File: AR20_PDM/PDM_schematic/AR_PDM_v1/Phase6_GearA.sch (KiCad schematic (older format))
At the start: 12 parts, among them Q5 BTS50025-1TAD, U10 N-MOS, U5 INA233

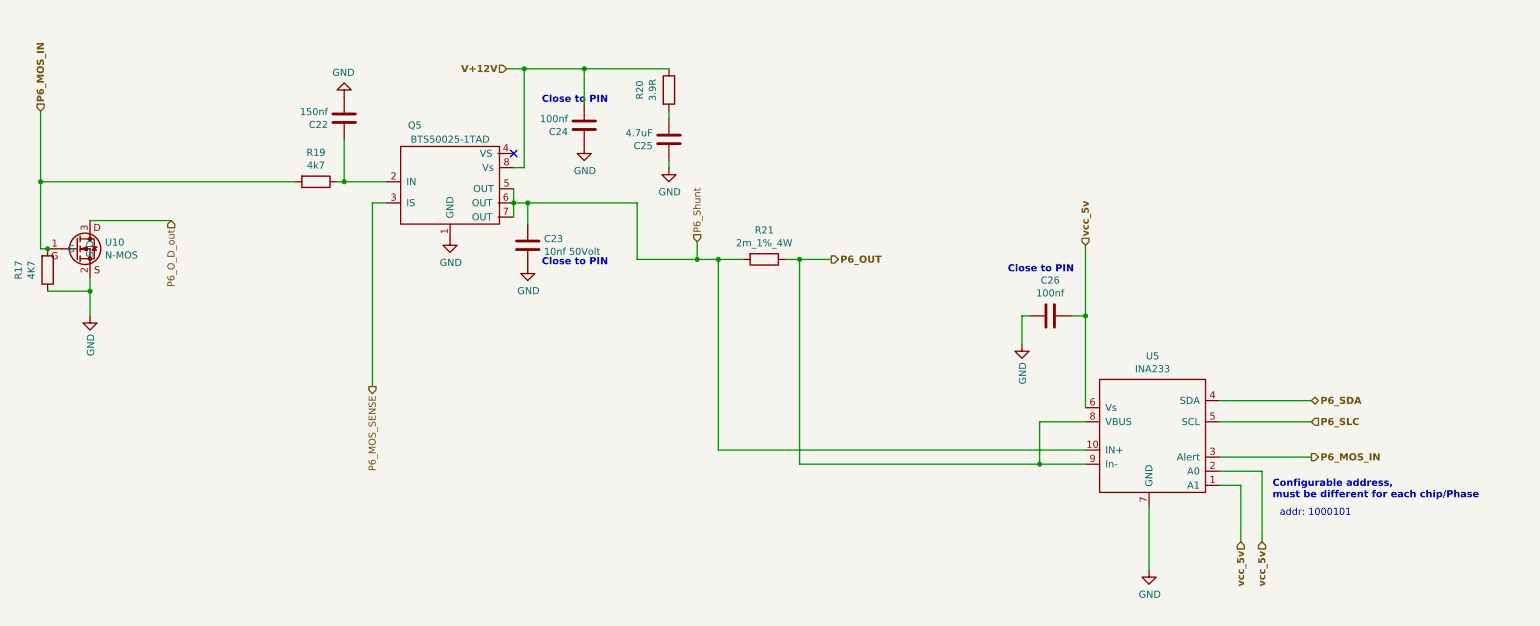
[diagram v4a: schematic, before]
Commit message: schematics rework
Fixed INA233 frying due to inductive flyback:
- Paced ina233 high side of the mosftets
- New input protection reseistors, and zener diodes, on each ina233.
Simplified:
- Removed the MUX and mos sense lines, as i realize that most of this functionality can be obtained trough INA233.
- Removed some of the cappacitors , besides the most needed ones.
- removed  back to back zener diode configuration, now a single diode insted.
 to reduce negative voltage in case of loss of VS, to be easy on the INA233 filters.
new stuff:
- Another temp sensor.
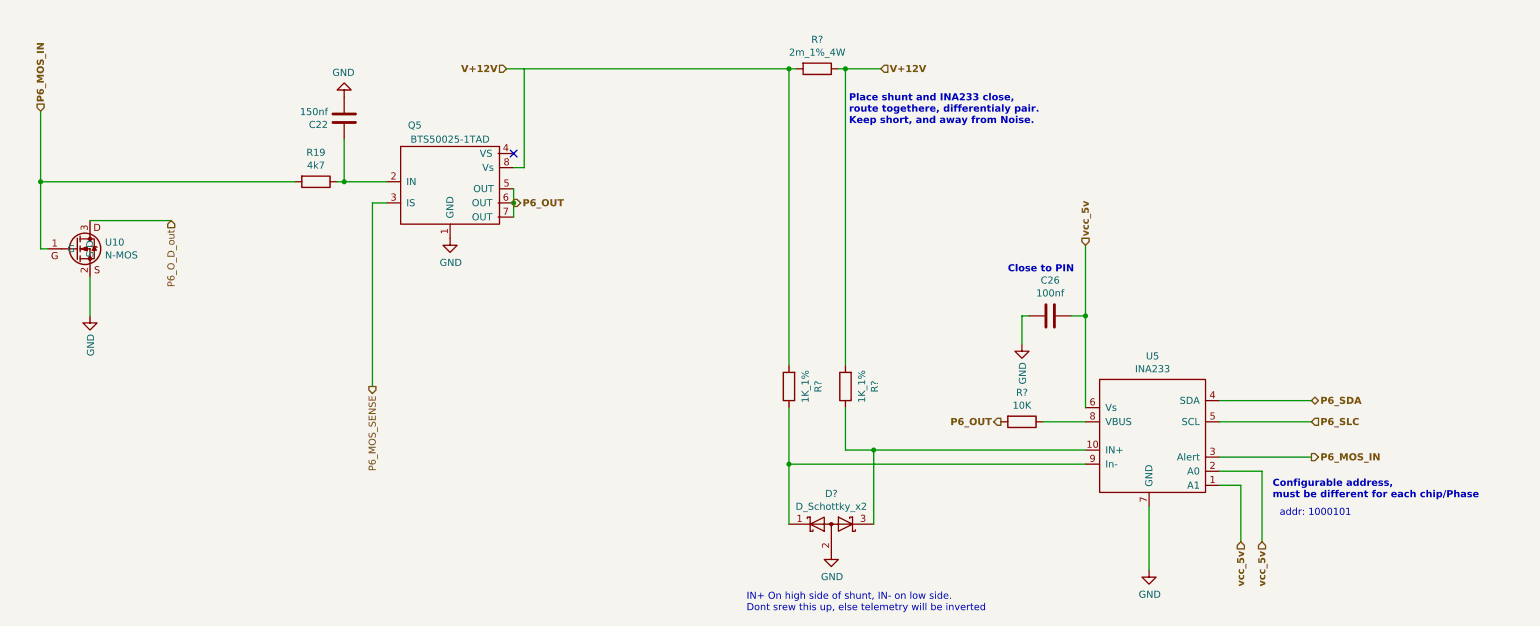
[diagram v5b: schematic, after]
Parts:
- removed C23: 10nf 50Volt, Capacitor_SMD:C_0603_1608Metric, symbol AR20_PDM_v1-rescue:C-Device
- removed C24: 100nf, Capacitor_SMD:C_0603_1608Metric, symbol AR20_PDM_v1-rescue:C-Device
- removed C25: 4.7uF, Capacitor_SMD:C_1206_3216Metric, symbol AR20_PDM_v1-rescue:C-Device
- removed R17: 4K7, Resistor_SMD:R_0603_1608Metric, symbol AR20_PDM_v1-rescue:R-Device
- removed R20: 3.9R, Resistor_SMD:R_2512_6332Metric, symbol AR20_PDM_v1-rescue:R-Device
- removed R21: 2m_1%_4W, Resistor_SMD:R_2512_6332Metric, symbol AR20_PDM_v1-rescue:R-Device
- added D?: D_Schottky_x2, symbol AR20_PDM_v1-rescue:D_Schottky_x2
- added R?: 2m_1%_4W, Resistor_SMD:R_2512_6332Metric, symbol AR20_PDM_v1-rescue:R-Device
- added R? (x2): 1K_1%, Resistor_SMD:R_0603_1608Metric, symbol AR20_PDM_v1-rescue:R-Device
- added R?: 10K, Resistor_SMD:R_0603_1608Metric, symbol AR20_PDM_v1-rescue:R-Device
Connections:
- net GND: now also D?.2 (A)
- net P6_OUT: now also Q5.5 (OUT), Q5.6 (OUT), Q5.7 (OUT), R?.2; no longer U5.8 (VBUS), U5.9 (In-)
- net V+12V: now also R?.1, R?.2, R?.2, R?.2
- removed net P6_Shunt: Q5.5 (OUT), Q5.6 (OUT), Q5.7 (OUT), U5.10 (IN+)
- new net: D?.3 (K), R?.1, U5.10 (IN+)
- new net: R?.1, U5.8 (VBUS)
- new net: D?.1 (K), R?.1, U5.9 (In-)
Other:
- note added: "IN+ On high side of shunt, IN- on low side.\nDont srew this up, else telemetry will be inverted"
- note added: "Place shunt and INA233 close, \nroute togethere, differentialy pair. \nKeep short, and away from Noise."

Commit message: Working on pcb layout
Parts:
- removed D?: D_Schottky_x2, symbol AR20_PDM_v1-rescue:D_Schottky_x2
- added D47, D49: D_Schottky_BAT60A, AR_PDM_v1:D_Shotky_BAT60_HandSoldering, symbol AR20_PDM_v1-rescue:D_Schottky_BAT60A
- gave numbers to parts that had none: 4
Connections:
- net GND: now also D47.2 (A), D49.2 (A)
- net V+12V: no longer Q5.8 (Vs), R32.2, R33.2
- net at R109.1, U5.10 (IN+): now also D49.1 (K)
- net at R32.1, U5.9 (In-): now also D47.1 (K)
- new net: Q5.8 (Vs), R32.2, R33.2
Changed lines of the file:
@@
 Connection ~ 1350 2400
-Wire Wire Line
-	4650 1600 4775 1600
 Wire Wire Line
 	4775 2300 4700 2300
@@
 Wire Wire Line
 	1700 3075 1700 3350
-Text HLabel 4650 1600 0    50   Input ~ 10
-V+12V
 Text HLabel 4700 2550 2    50   Output ~ 10
 P6_OUT
@@
 AR Path="/5E0FC3A2/5EEB3767" Ref="R?"  Part="1"
 AR Path="/5E0FCFDC/5EEB3767" Ref="R?"  Part="1"
-AR Path="/5E0FDCCC/5EEB3767" Ref="R?"  Part="1"
+AR Path="/5E0FDCCC/5EEB3767" Ref="R33"  Part="1"
 AR Path="/5E10174B/5EEB3767" Ref="R?"  Part="1"
-F 0 "R?" V 6643 1600 50  0000 C CNN
+F 0 "R33" V 6643 1600 50  0000 C CNN
 F 1 "2m_1%_4W" V 6734 1600 50  0000 C CNN
 F 2 "Resistor_SMD:R_2512_6332Metric" V 6780 1600 50  0001 C CNN
@@
 Text HLabel 7300 1600 2    50   Input ~ 10
 V+12V
-$Comp
-L AR20_PDM_v1-rescue:D_Schottky_x2 D?
-U 1 1 5EEB376E
-P 6950 4825
-AR Path="/5DA89415/5EEB376E" Ref="D?"  Part="1"
-AR Path="/5E0FDCCC/5EEB376E" Ref="D?"  Part="1"
-F 0 "D?" H 6950 5041 50  0000 C CNN
-F 1 "D_Schottky_x2" H 6950 4950 50  0000 C CNN
-F 2 "" H 6950 4825 50  0001 C CNN
-F 3 "~" H 6950 4825 50  0001 C CNN
-	1    6950 4825
-	1    0    0    -1
-$EndComp
 $Comp
 L AR20_PDM_v1-rescue:R-Device R?
@@
 AR Path="/5E0FC3A2/5EEB3774" Ref="R?"  Part="1"
 AR Path="/5E0FCFDC/5EEB3774" Ref="R?"  Part="1"
-AR Path="/5E0FDCCC/5EEB3774" Ref="R?"  Part="1"
+AR Path="/5E0FDCCC/5EEB3774" Ref="R32"  Part="1"
 AR Path="/5E10174B/5EEB3774" Ref="R?"  Part="1"
-F 0 "R?" V 6443 3850 50  0000 C CNN
+F 0 "R32" V 6443 3850 50  0000 C CNN
 F 1 "1K_1%" V 6534 3850 50  0000 C CNN
 F 2 "Resistor_SMD:R_0603_1608Metric" V 6580 3850 50  0001 C CNN
@@
 AR Path="/5E0FC3A2/5EEB377A" Ref="R?"  Part="1"
 AR Path="/5E0FCFDC/5EEB377A" Ref="R?"  Part="1"
-AR Path="/5E0FDCCC/5EEB377A" Ref="R?"  Part="1"
+AR Path="/5E0FDCCC/5EEB377A" Ref="R109"  Part="1"
 AR Path="/5E10174B/5EEB377A" Ref="R?"  Part="1"
-F 0 "R?" V 6843 3850 50  0000 C CNN
+F 0 "R109" V 6843 3850 50  0000 C CNN
 F 1 "1K_1%" V 6934 3850 50  0000 C CNN
 F 2 "Resistor_SMD:R_0603_1608Metric" V 6980 3850 50  0001 C CNN
@@
 Text Notes 7075 2000 0    50   ~ 10
 Place shunt and INA233 close, \nroute togethere, differentialy pair. \nKeep short, and away from Noise.
-$Comp
-L AR20_PDM_v1-rescue:GND-power #PWR?
-U 1 1 5EEB3788
-P 6950 5025
-AR Path="/5DA89415/5EEB3788" Ref="#PWR?"  Part="1"
-AR Path="/5DEB10A1/5EEB3788" Ref="#PWR?"  Part="1"
-AR Path="/5DEB20EA/5EEB3788" Ref="#PWR?"  Part="1"
-AR Path="/5E0E4725/5EEB3788" Ref="#PWR?"  Part="1"
-AR Path="/5E0E4A93/5EEB3788" Ref="#PWR?"  Part="1"
-AR Path="/5E0E4EB5/5EEB3788" Ref="#PWR?"  Part="1"
-AR Path="/5E0E5304/5EEB3788" Ref="#PWR?"  Part="1"
-AR Path="/5E0E594B/5EEB3788" Ref="#PWR?"  Part="1"
-AR Path="/5E0E607C/5EEB3788" Ref="#PWR?"  Part="1"
-AR Path="/5E0FB5C8/5EEB3788" Ref="#PWR?"  Part="1"
-AR Path="/5E0FBBBD/5EEB3788" Ref="#PWR?"  Part="1"
-AR Path="/5E0FC3A2/5EEB3788" Ref="#PWR?"  Part="1"
-AR Path="/5E0FCFDC/5EEB3788" Ref="#PWR?"  Part="1"
-AR Path="/5E0FDCCC/5EEB3788" Ref="#PWR?"  Part="1"
-AR Path="/5E10174B/5EEB3788" Ref="#PWR?"  Part="1"
-F 0 "#PWR?" H 6950 4775 50  0001 C CNN
-F 1 "GND" H 6955 4852 50  0000 C CNN
-F 2 "" H 6950 5025 50  0001 C CNN
-F 3 "" H 6950 5025 50  0001 C CNN
-	1    6950 5025
-	1    0    0    -1
-$EndComp
 Wire Wire Line
 	4775 1600 6650 1600
@@
 Wire Wire Line
 	6650 4400 8750 4400
-Connection ~ 6650 4400
-Wire Wire Line
-	6650 4400 6650 4825
-Wire Wire Line
-	8750 4300 7250 4300
-Wire Wire Line
-	7250 4825 7250 4300
-Connection ~ 7250 4300
-Wire Wire Line
-	7250 4300 7050 4300
 $Comp
 L AR20_PDM_v1-rescue:R-Device R?
@@
 AR Path="/5E0FC3A2/5EEC7147" Ref="R?"  Part="1"
 AR Path="/5E0FCFDC/5EEC7147" Ref="R?"  Part="1"
-AR Path="/5E0FDCCC/5EEC7147" Ref="R?"  Part="1"
+AR Path="/5E0FDCCC/5EEC7147" Ref="R110"  Part="1"
 AR Path="/5E10174B/5EEC7147" Ref="R?"  Part="1"
-F 0 "R?" V 8093 4100 50  0000 C CNN
+F 0 "R110" V 8093 4100 50  0000 C CNN
 F 1 "10K" V 8184 4100 50  0000 C CNN
 F 2 "Resistor_SMD:R_0603_1608Metric" V 8230 4100 50  0001 C CNN
@@
 Text HLabel 8150 4100 0    50   Output ~ 10
 P6_OUT
+Wire Wire Line
+	7050 4300 7100 4300
+$Comp
+L AR20_PDM_v1-rescue:D_Schottky_BAT60A D?
+U 1 1 5EFB12F9
+P 6700 4775
+AR Path="/5DA89415/5EFB12F9" Ref="D?"  Part="1"
+AR Path="/5E0FDCCC/5EFB12F9" Ref="D47"  Part="1"
+F 0 "D47" V 6530 4885 50  0000 L CNN
+F 1 "D_Schottky_BAT60A" V 6621 4885 50  0000 L CNN
+F 2 "AR_PDM_v1:D_Shotky_BAT60_HandSoldering" H 6800 4725 50  0001 C CNN
+F 3 "~" H 6800 4725 50  0001 C CNN
+	1    6700 4775
+	0    1    1    0
+$EndComp
+$Comp
+L AR20_PDM_v1-rescue:GND-power #PWR?
+U 1 1 5EFB12FF
+P 6875 4950
+AR Path="/5DA89415/5EFB12FF" Ref="#PWR?"  Part="1"
+AR Path="/5DEB10A1/5EFB12FF" Ref="#PWR?"  Part="1"
+AR Path="/5DEB20EA/5EFB12FF" Ref="#PWR?"  Part="1"
+AR Path="/5E0E4725/5EFB12FF" Ref="#PWR?"  Part="1"
+AR Path="/5E0E4A93/5EFB12FF" Ref="#PWR?"  Part="1"
+AR Path="/5E0E4EB5/5EFB12FF" Ref="#PWR?"  Part="1"
+AR Path="/5E0E5304/5EFB12FF" Ref="#PWR?"  Part="1"
+AR Path="/5E0E594B/5EFB12FF" Ref="#PWR?"  Part="1"
+AR Path="/5E0E607C/5EFB12FF" Ref="#PWR?"  Part="1"
+AR Path="/5E0FB5C8/5EFB12FF" Ref="#PWR?"  Part="1"
+AR Path="/5E0FBBBD/5EFB12FF" Ref="#PWR?"  Part="1"
+AR Path="/5E0FC3A2/5EFB12FF" Ref="#PWR?"  Part="1"
+AR Path="/5E0FCFDC/5EFB12FF" Ref="#PWR?"  Part="1"
+AR Path="/5E0FDCCC/5EFB12FF" Ref="#PWR011"  Part="1"
+AR Path="/5E10174B/5EFB12FF" Ref="#PWR?"  Part="1"
+F 0 "#PWR011" H 6875 4700 50  0001 C CNN
+F 1 "GND" H 6880 4777 50  0000 C CNN
+F 2 "" H 6875 4950 50  0001 C CNN
+F 3 "" H 6875 4950 50  0001 C CNN
+	1    6875 4950
+	1    0    0    -1
+$EndComp
+$Comp
+L AR20_PDM_v1-rescue:D_Schottky_BAT60A D?
+U 1 1 5EFB1305
+P 7150 4775
+AR Path="/5DA89415/5EFB1305" Ref="D?"  Part="1"
+AR Path="/5E0FDCCC/5EFB1305" Ref="D49"  Part="1"
+F 0 "D49" V 6980 4885 50  0000 L CNN
+F 1 "D_Schottky_BAT60A" V 7071 4885 50  0000 L CNN
+F 2 "AR_PDM_v1:D_Shotky_BAT60_HandSoldering" H 7250 4725 50  0001 C CNN
+F 3 "~" H 7250 4725 50  0001 C CNN
+	1    7150 4775
+	0    1    1    0
+$EndComp
+Wire Wire Line
+	6650 4475 6650 4400
+Wire Wire Line
+	7100 4475 7100 4300
+Wire Wire Line
+	6650 4825 6875 4825
+Wire Wire Line
+	6875 4950 6875 4825
+Connection ~ 6875 4825
+Wire Wire Line
+	6875 4825 7100 4825
+Connection ~ 7100 4300
+Wire Wire Line
+	7100 4300 8750 4300
+Connection ~ 6650 4400
 $EndSCHEMATC

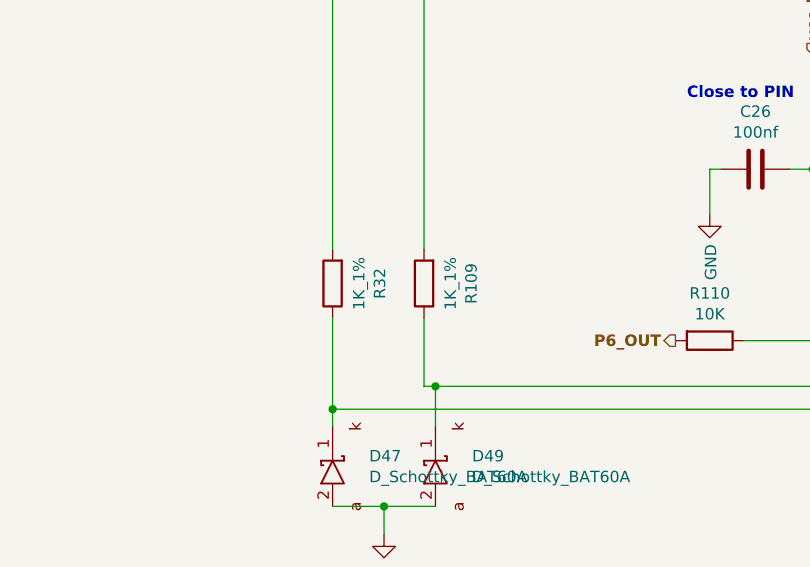
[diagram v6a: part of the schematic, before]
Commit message: shematics adjustments, and fixing values and names
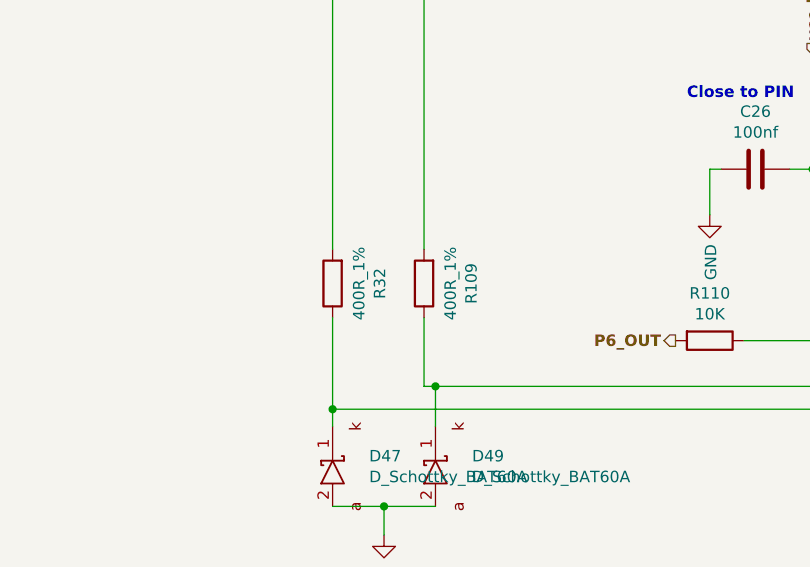
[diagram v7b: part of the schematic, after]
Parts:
- R109, R32: value 1K_1% -> 400R_1%
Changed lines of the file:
@@
 AR Path="/5E10174B/5EEB3774" Ref="R?"  Part="1"
 F 0 "R32" V 6443 3850 50  0000 C CNN
-F 1 "1K_1%" V 6534 3850 50  0000 C CNN
+F 1 "400R_1%" V 6534 3850 50  0000 C CNN
 F 2 "Resistor_SMD:R_0603_1608Metric" V 6580 3850 50  0001 C CNN
 F 3 "~" H 6650 3850 50  0001 C CNN
@@
 AR Path="/5E10174B/5EEB377A" Ref="R?"  Part="1"
 F 0 "R109" V 6843 3850 50  0000 C CNN
-F 1 "1K_1%" V 6934 3850 50  0000 C CNN
+F 1 "400R_1%" V 6934 3850 50  0000 C CNN
 F 2 "Resistor_SMD:R_0603_1608Metric" V 6980 3850 50  0001 C CNN
 F 3 "~" H 7050 3850 50  0001 C CNN
